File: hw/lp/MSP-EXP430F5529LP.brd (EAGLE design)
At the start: 201.6 x 48.2 mm, 27 parts, among them J10 PWR, J3 PWR, Q2 32.768kHz, Q4 CSTCR4M00G15L99, U6 MSP430F5529IPNR

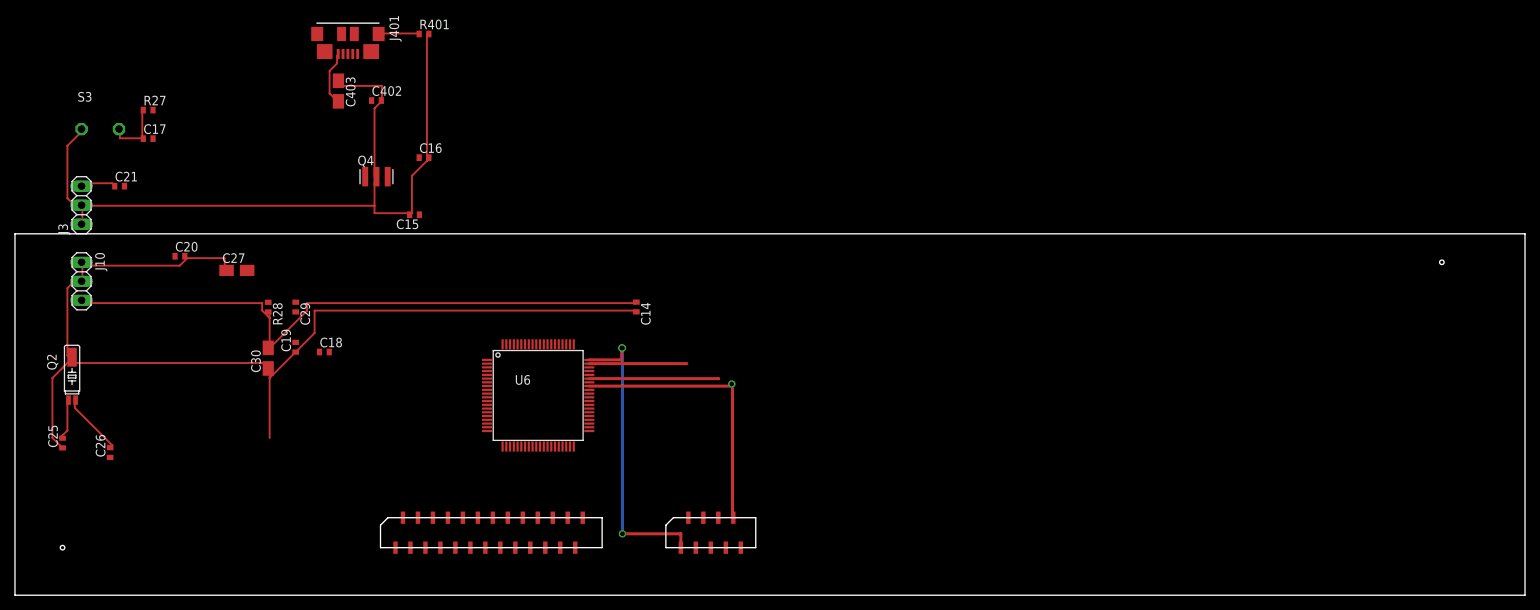
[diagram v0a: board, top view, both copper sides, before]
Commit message: adding usb power need ldos
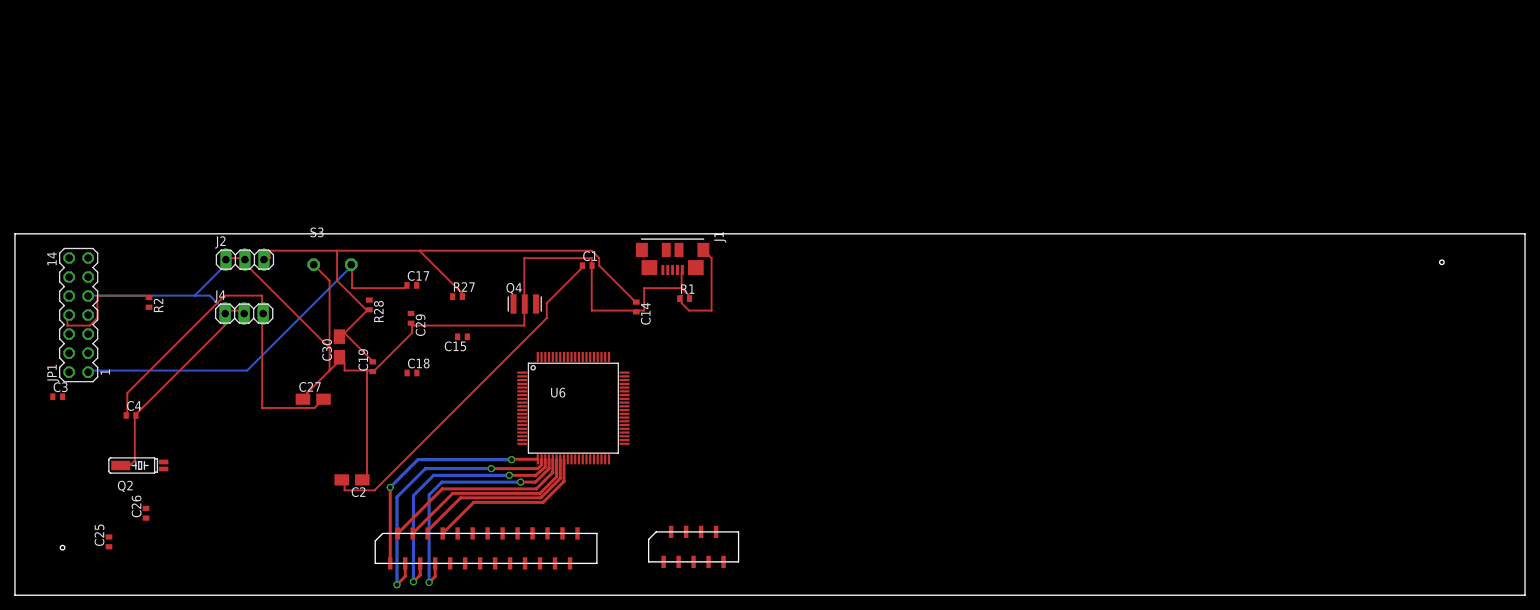
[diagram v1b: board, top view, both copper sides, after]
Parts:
- removed C16: 220n, rcl:C0402
- removed C20, C21, C402: 100n, rcl:C0402
- removed C403: 4u7, rcl:A/3216-18R
- removed J10, J3: PWR, pinhead:1X03
- removed J401: (no value), usb_con-update:HIROSE-ZX62R-B-5P
- removed R401: 33R, rcl:R0402
- added C1, C3, C4: 100n, rcl:C0402
- added C2: 4u7, rcl:A/3216-18R
- added J1: (no value), usb_con-update:HIROSE-ZX62R-B-5P
- added J2, J4: PWR, pinhead:1X03
- added JP1: JTAG, con-lstb:MA07-2
- added R1: 33R, rcl:R0402
- added R2: 330R, rcl:R0402
- moved R27 48.2 mm to (59.1, 39.9)
- moved C17 40.3 mm to (53.0, 41.4)
- moved S3 35.9 mm to (39.9, 44.1)
- moved Q4 26.1 mm to (68.1, 38.9)
- moved C27 20.0 mm to (39.8, 26.2)
- moved C15 17.5 mm to (59.7, 34.5)
- moved C29 15.5 mm to (52.9, 37.0)
- moved Q2 15.3 mm to (15.4, 17.3), turned to 90 degrees
- moved C25 14.6 mm to (12.6, 7.12)
- moved R28 13.5 mm to (47.3, 38.8)
- moved C18 12.0 mm to (53.0, 29.7)
- moved C19 10.6 mm to (47.8, 30.5)
- moved C30 9.62 mm to (43.3, 33.1)
- moved C26 9.42 mm to (17.5, 10.9)
- moved U6 5.00 mm to (74.5, 25.0)
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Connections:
- removed net EZFET_VBUS: C402.1, C403.+, J401.VBUS
- removed net N$10: J401.SHIELD1, R401.1
- removed net N$11: U$2.P13
- removed net N$12: J401.D+
- removed net N$13: J401.D-
- removed net N$14: U$2.P12
- removed net N$15: U$2.P11
- removed net N$16: U$2.P10
- removed net N$17: U$2.P9
- removed net N$18: U$2.P8
- removed net N$19: U$2.P7
- removed net N$2: U$2.P2
- removed net N$20: U$2.P6
- removed net N$21: U$2.P5
- removed net N$22: U$2.P4
- removed net N$23: U$2.P3
- removed net N$24: U$2.P21
- removed net N$25: U$2.P22
- removed net N$26: U$2.P23
- removed net N$27: U$2.P24
- removed net N$28: U$2.P25
- removed net N$29: U$2.P26
- removed net N$3: U$2.P18
- removed net N$4: U$2.P20
- removed net N$5: U$2.P17
- removed net N$6: U$2.P16
- removed net N$7: U$2.P15
- removed net N$8: U$2.P14
- removed net TARGET_VUSB: C16.1, U6.66
- new net DM: J1.D-, U6.64
- new net DP: J1.D+, U6.62
- new net N$39: J1.SHIELD1, R1.1
- new net SBWVCC: JP1.2
- new net VUSB: C1.1, C2.+, J1.VBUS, U6.66
- net +3V3: now also C3.1, J2.3; no longer C20.1, J10.3
- net +5V: now also C4.1, J4.3; no longer C21.1, J3.3
- net GND: now also C1.2, C2.-, C3.2, C4.2, J1.GND, J2.1, J2.2, J4.1, J4.2, JP1.9, R1.2; no longer C16.2, C20.2, C21.2, C402.2, C403.-, J10.1, J10.2, J3.1, J3.2, J401.GND, R401.2
- net N$1: now also JP1.7, R2.2; no longer U$2.P1
- net P1.0: now also U$2.P1
- net P1.1: now also U$2.P3
- net P1.2: now also U$2.P5
- net P1.3: now also U$2.P7
- net P1.4: now also U$2.P2
- net P1.5: now also U$2.P4
- net P1.6: now also U$2.P6
- net P1.7: now also U$2.P8
- net P2.0: now also U$2.P9
- net P2.1: now also U$2.P10
- net P2.2: now also U$2.P11
- net P2.3: now also U$2.P12
- net P2.4: now also U$2.P13
- net P2.5: now also U$2.P14
- net P2.6: now also U$2.P15
- net P2.7: now also U$2.P16
- net P3.0: now also U$2.P17
- net P3.1: now also U$2.P18
- net P3.2: now also U$2.P20
- net P3.3: now also U$2.P21
- net P3.4: now also U$2.P22
- net P3.5: now also U$2.P23
- net P3.6: now also U$2.P24
- net P3.7: now also U$2.P25
- net P4.0: now also U$2.P26
- net RST/SBWTDIO: now also JP1.1
- net TEST/SBWTCK: now also JP1.8, R2.1
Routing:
- net GND: track 250.8 -> 187.7 mm
- net VUSB: track 0.00 -> 47.4 mm
- net +5V: track 4.91 -> 50.2 mm
- net RST/SBWTDIO: track 8.66 -> 51.9 mm
- net N$9: track 40.5 -> 0.00 mm, vias 2 -> 0
- net N$36: track 37.0 -> 0.00 mm
- net P1.1: track 0.00 -> 36.8 mm, vias 0 -> 2
- net P1.2: track 0.00 -> 34.5 mm, vias 0 -> 2
- net P1.3: track 0.00 -> 33.3 mm, vias 0 -> 2
- net P1.0: track 0.00 -> 31.4 mm, vias 0 -> 2
- net P1.4: track 0.00 -> 25.8 mm
- net P1.5: track 0.00 -> 24.7 mm
- net P1.6: track 0.00 -> 23.5 mm
- net P1.7: track 0.00 -> 22.0 mm
- net N$34: track 17.2 -> 0.00 mm
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
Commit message: figuring out a pattern for matrix scanning
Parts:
- moved U6 4.40 mm to (74.5, 29.4)
- moved U$1 1.73 mm to (84.9, 4.15)
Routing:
- net TEST/SBWTCK: track 16.1 -> 94.4 mm, vias 0 -> 1
- net N$9: track 0.00 -> 65.1 mm
- net GND: track 187.7 -> 244.9 mm, vias 0 -> 4
- net +3V3: track 84.2 -> 141.4 mm
- net +5V: track 50.2 -> 103.9 mm, vias 0 -> 1
- net RST/SBWTDIO: track 51.9 -> 94.6 mm, vias 0 -> 1
- net N$35: track 0.00 -> 41.0 mm, vias 0 -> 2
- net N$31: track 0.00 -> 40.8 mm, vias 0 -> 2
- net N$33: track 0.00 -> 39.8 mm, vias 0 -> 2
- net N$36: track 0.00 -> 32.9 mm
- net N$34: track 0.00 -> 32.1 mm, vias 0 -> 2
- net P3.7: track 0.00 -> 31.3 mm, vias 0 -> 1
- net N$32: track 0.00 -> 29.4 mm, vias 0 -> 2
- net P3.5: track 0.00 -> 29.0 mm, vias 0 -> 1
- net P4.0: track 0.00 -> 26.4 mm, vias 0 -> 1
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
